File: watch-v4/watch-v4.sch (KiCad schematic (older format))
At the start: 33 parts, among them J1 CONN_10, P1 array connection, Q1 MOSFET_P, SW1 SPST, SW2 SPST, SW3 SPST, U1 IC_MCP73831, U2 MAX1722, U3 DS3231, U4 LSM9DS0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

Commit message: schematic cleanup, board work
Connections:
- net EXTVCC: now also D1.1 (A), R3.1
- net VCC: now also J1.4 (P4)
- net STAT: now reaches D2.2 (A), U1.1 (STAT)
- net Regulator_In: now reaches D1.2 (K), L1.1, Q1.3 (S), U2.1 (VIN)
- net Regulator_In: now also U2.3 (FB)
- net at C10.1, X1.3: now also U5.38 (XC1); no longer U5.37 (XC2)
- net at 12pf1.2, X1.1: now also U5.37 (XC2); no longer U5.38 (XC1)
- no-connect marks 1 -> 0
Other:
- moved on the sheet: C5, C6, C7, C8, D1, D2, L1, LIPOLY1, Q1, R1, R2, R3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

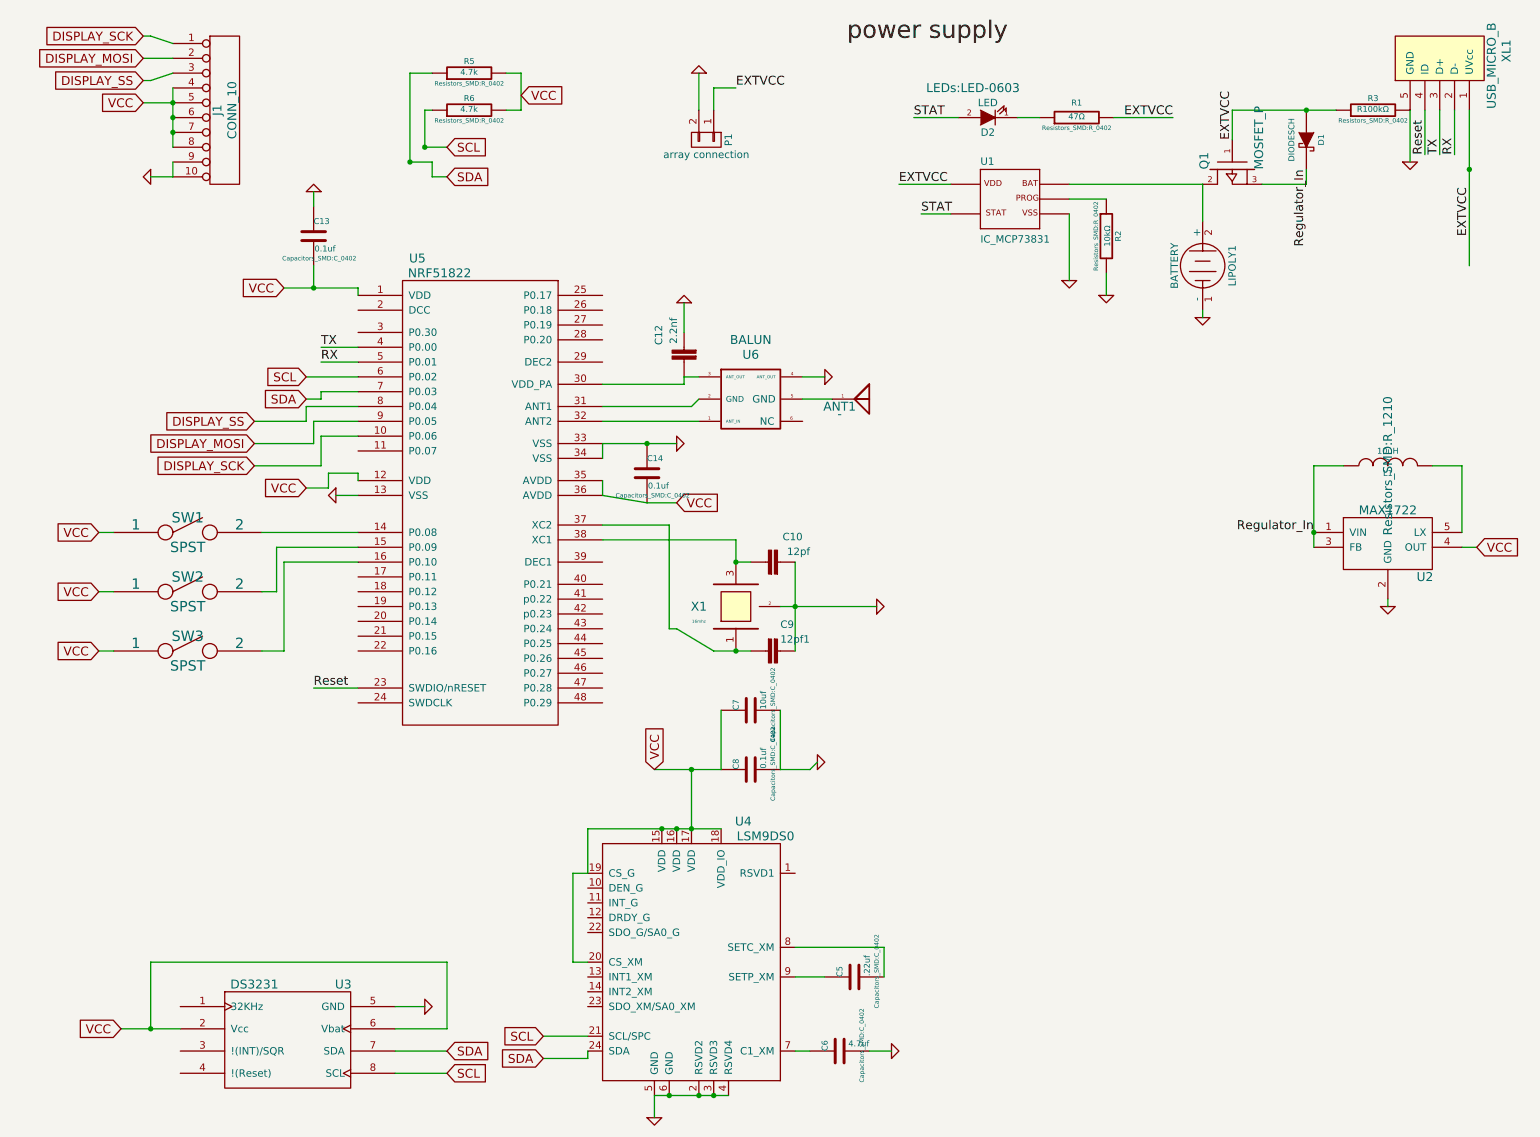
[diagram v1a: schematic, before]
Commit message: re-route board, redraw power supply in schematic
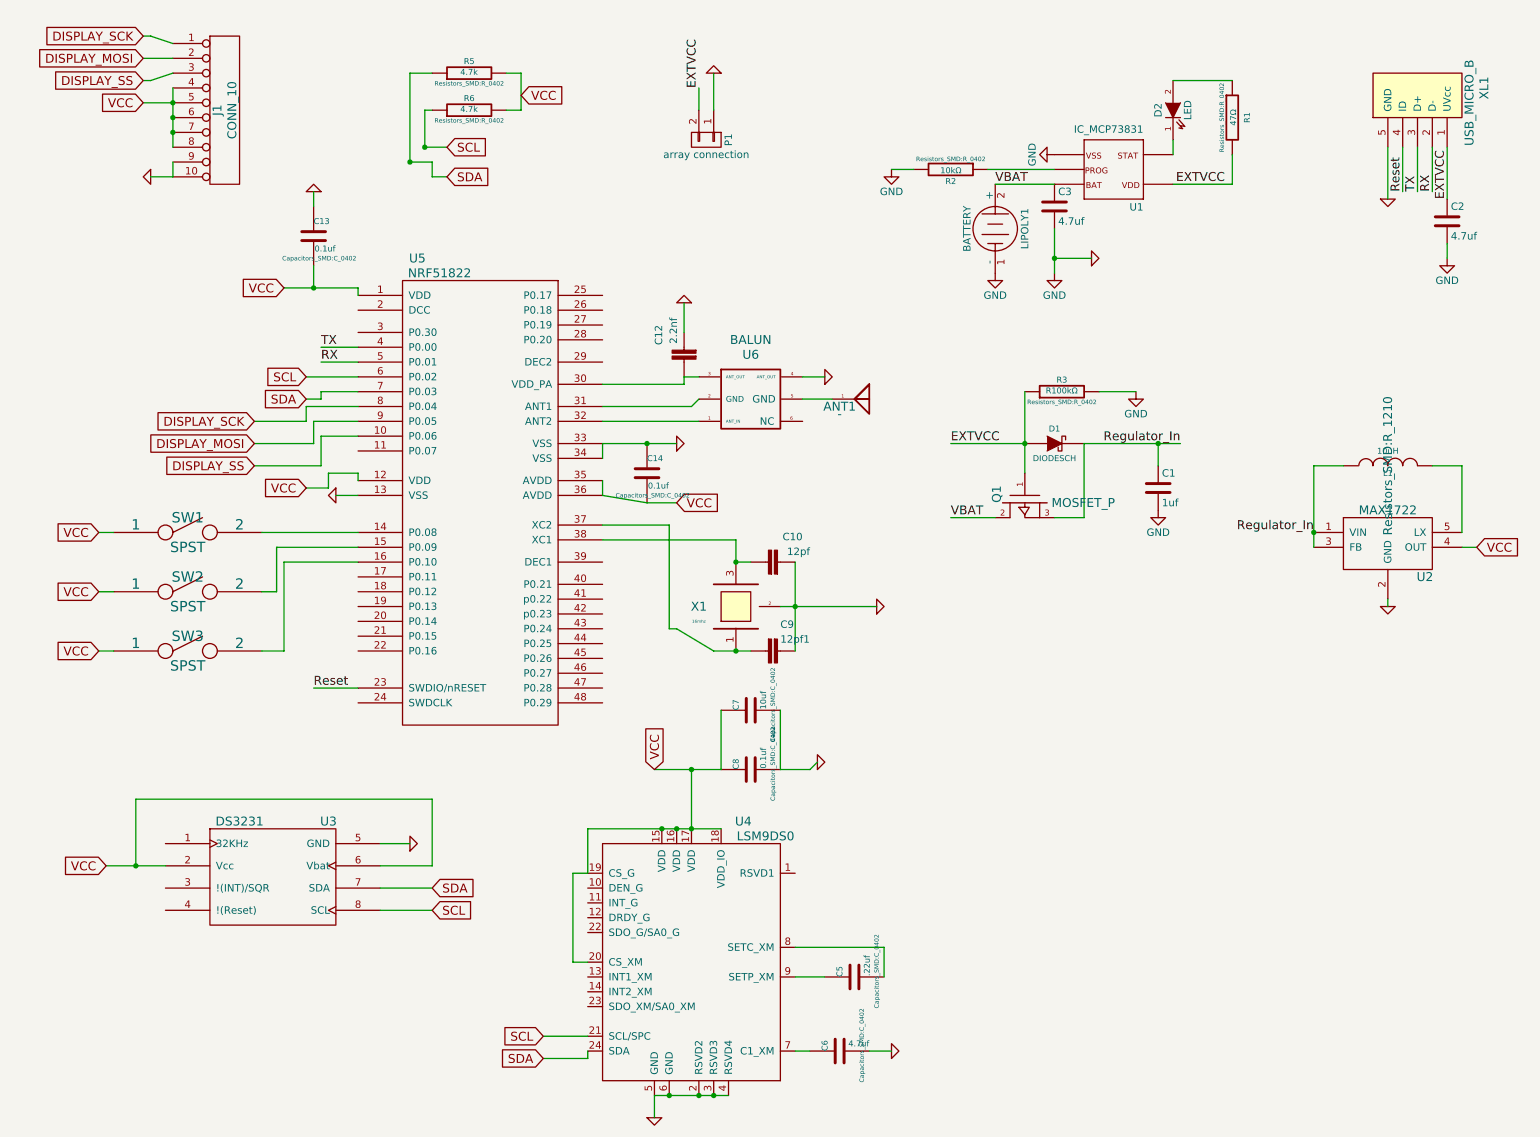
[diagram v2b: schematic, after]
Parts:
- added C1: 1uf, symbol C
- added C2, C3: 4.7uf, symbol C
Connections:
- net DISPLAY_SCK: now also U5.8 (P0.04); no longer U5.10 (P0.06)
- net DISPLAY_SS: now also U5.10 (P0.06); no longer U5.8 (P0.04)
- net EXTVCC: now also P1.2 (P2), C2.1; no longer P1.1 (P1)
- net GND: now also P1.1 (P1), C1.2, C2.2, C3.2; no longer P1.2 (P2)
- net Regulator_In: now also C1.1
- net VBAT: now reaches LIPOLY1.2 (+), Q1.2 (D), U1.3 (BAT)
- net VBAT: now also C3.1
- net at D2.1 (K): now also U1.1 (STAT); no longer R1.1
- net STAT: no longer names the net of D2.2 (A)
- net STAT: now also R1.1; no longer U1.1 (STAT)
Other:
- moved on the sheet: D1, D2, LIPOLY1, Q1, R1, R2, R3, U1, U3, XL1

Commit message: forgot to netlist the new parts; now with more caps, connections
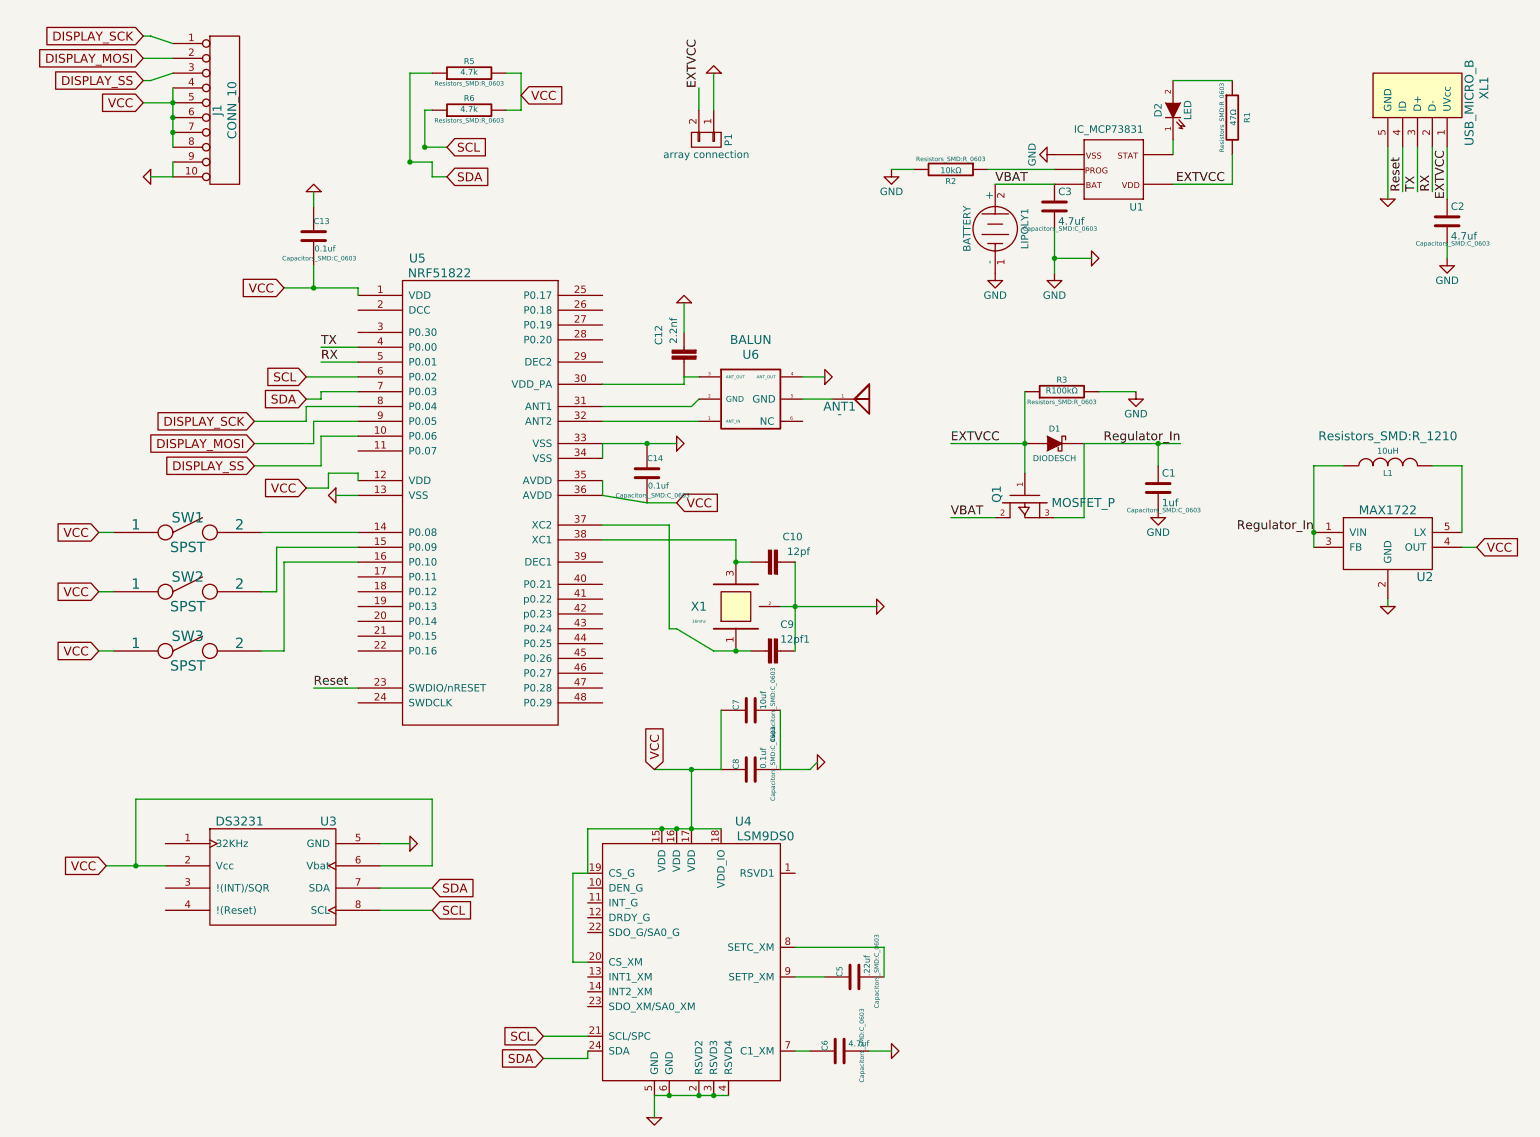
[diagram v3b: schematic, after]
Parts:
- 12pf1, C10, C12, C13, C14, C5, C6, C7, C8: footprint Capacitors_SMD:C_0402 -> Capacitors_SMD:C_0603
- C1, C2, C3: footprint (none) -> Capacitors_SMD:C_0603
- D1: footprint Diodes_SMD:Diode-SMA_Standard -> Diodes_SMD:SOD-123
- J1: footprint watch-v4:omron_XF2M-1015-1A -> watch-v4:omron_XF2M-1015-1A-2
- R1, R2, R3, R5, R6: footprint Resistors_SMD:R_0402 -> Resistors_SMD:R_0603
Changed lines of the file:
@@
 F 0 "R2" V 6730 1500 40  0000 C CNN
 F 1 "10kΩ" V 6657 1501 40  0000 C CNN
-F 2 "Resistors_SMD:R_0402" V 6580 1500 30  0000 C CNN
+F 2 "Resistors_SMD:R_0603" V 6580 1500 30  0000 C CNN
 F 3 "~" H 6650 1500 30  0000 C CNN
 	1    6650 1500
@@
 F 0 "R1" V 8650 1150 40  0000 C CNN
 F 1 "47Ω" V 8557 1151 40  0000 C CNN
-F 2 "Resistors_SMD:R_0402" V 8480 1150 30  0000 C CNN
+F 2 "Resistors_SMD:R_0603" V 8480 1150 30  0000 C CNN
 F 3 "~" H 8550 1150 30  0000 C CNN
 	1    8550 1150
@@
 F 0 "D1" H 7350 3450 40  0000 C CNN
 F 1 "DIODESCH" H 7350 3250 40  0000 C CNN
-F 2 "Diodes_SMD:Diode-SMA_Standard" H 7350 3350 60  0001 C CNN
+F 2 "Diodes_SMD:SOD-123" H 7350 3350 60  0001 C CNN
 F 3 "~" H 7350 3350 60  0000 C CNN
 	1    7350 3350
@@
 F 0 "R3" V 7480 3000 40  0000 C CNN
 F 1 "R100kΩ" V 7407 3001 40  0000 C CNN
-F 2 "Resistors_SMD:R_0402" V 7330 3000 30  0000 C CNN
+F 2 "Resistors_SMD:R_0603" V 7330 3000 30  0000 C CNN
 F 3 "~" H 7400 3000 30  0000 C CNN
 	1    7400 3000
@@
 F 0 "L1" V 9550 3500 40  0000 C CNN
 F 1 "10uH" V 9700 3500 40  0000 C CNN
-F 2 "Resistors_SMD:R_1210" H 9600 3500 60  0000 C CNN
+F 2 "Resistors_SMD:R_1210" V 9800 3500 60  0000 C CNN
 F 3 "~" H 9600 3500 60  0000 C CNN
 	1    9600 3500
@@
 F 0 "R5" V 3480 850 40  0000 C CNN
 F 1 "4.7k" V 3407 851 40  0000 C CNN
-F 2 "Resistors_SMD:R_0402" V 3330 850 30  0000 C CNN
+F 2 "Resistors_SMD:R_0603" V 3330 850 30  0000 C CNN
 F 3 "~" H 3400 850 30  0000 C CNN
 	1    3400 850
@@
 F 0 "R6" V 3480 1100 40  0000 C CNN
 F 1 "4.7k" V 3407 1101 40  0000 C CNN
-F 2 "Resistors_SMD:R_0402" V 3330 1100 30  0000 C CNN
+F 2 "Resistors_SMD:R_0603" V 3330 1100 30  0000 C CNN
 F 3 "~" H 3400 1100 30  0000 C CNN
 	1    3400 1100
@@
 F 0 "C5" H 6000 7050 40  0000 L CNN
 F 1 ".22uf" H 6006 6865 40  0000 L CNN
-F 2 "Capacitors_SMD:C_0402" H 6038 6800 30  0000 C CNN
+F 2 "Capacitors_SMD:C_0603" H 6038 6800 30  0000 C CNN
 F 3 "~" H 6000 6950 60  0000 C CNN
 	1    6000 6950
@@
 F 0 "C6" H 5900 7550 40  0000 L CNN
 F 1 "4.7uf" V 5950 7250 40  0000 L CNN
-F 2 "Capacitors_SMD:C_0402" H 5938 7300 30  0000 C CNN
+F 2 "Capacitors_SMD:C_0603" H 5938 7300 30  0000 C CNN
 F 3 "~" H 5900 7450 60  0000 C CNN
 	1    5900 7450
@@
 F 0 "C7" H 5300 5250 40  0000 L CNN
 F 1 "10uf" H 5306 5065 40  0000 L CNN
-F 2 "Capacitors_SMD:C_0402" H 5338 5000 30  0000 C CNN
+F 2 "Capacitors_SMD:C_0603" H 5338 5000 30  0000 C CNN
 F 3 "~" H 5300 5150 60  0000 C CNN
 	1    5300 5150
@@
 F 0 "C8" H 5300 5650 40  0000 L CNN
 F 1 "0.1uf" H 5306 5465 40  0000 L CNN
-F 2 "Capacitors_SMD:C_0402" H 5338 5400 30  0000 C CNN
+F 2 "Capacitors_SMD:C_0603" H 5338 5400 30  0000 C CNN
 F 3 "~" H 5300 5550 60  0000 C CNN
 	1    5300 5550
@@
 F 0 "J1" V 1700 1100 60  0000 C CNN
 F 1 "CONN_10" V 1800 1100 60  0000 C CNN
-F 2 "watch-v4:omron_XF2M-1015-1A" H 1750 1100 60  0001 C CNN
+F 2 "watch-v4:omron_XF2M-1015-1A-2" H 1750 1100 60  0001 C CNN
 F 3 "" H 1750 1100 60  0000 C CNN
 	1    1750 1100
@@
 F 0 "C10" V 5700 4000 50  0000 L BNN
 F 1 "12pf" V 5600 3950 50  0000 L BNN
-F 2 "Capacitors_SMD:C_0402" H 5500 4300 50  0001 C CNN
+F 2 "Capacitors_SMD:C_0603" H 5500 4300 50  0001 C CNN
 F 3 "" H 5500 4150 60  0000 C CNN
 	1    5500 4150
@@
 F 0 "12pf1" V 5350 4850 50  0000 L BNN
 F 1 "C9" V 5250 4850 50  0000 L BNN
-F 2 "Capacitors_SMD:C_0402" H 5400 4900 50  0001 C CNN
+F 2 "Capacitors_SMD:C_0603" H 5400 4900 50  0001 C CNN
 F 3 "" H 5400 4750 60  0000 C CNN
 	1    5400 4750
@@
 F 0 "C12" V 5050 2550 50  0000 L BNN
 F 1 "2.2nf" V 4950 2500 50  0000 L BNN
-F 2 "Capacitors_SMD:C_0402" H 4850 2850 50  0001 C CNN
+F 2 "Capacitors_SMD:C_0603" H 4850 2850 50  0001 C CNN
 F 3 "" H 4850 2700 60  0000 C CNN
 	1    4850 2700
@@
 F 0 "C13" H 2350 2050 40  0000 L CNN
 F 1 "0.1uf" H 2356 1865 40  0000 L CNN
-F 2 "Capacitors_SMD:C_0402" H 2388 1800 30  0000 C CNN
+F 2 "Capacitors_SMD:C_0603" H 2388 1800 30  0000 C CNN
 F 3 "~" H 2350 1950 60  0000 C CNN
 	1    2350 1950
@@
 F 0 "C14" H 4600 3650 40  0000 L CNN
 F 1 "0.1uf" H 4606 3465 40  0000 L CNN
-F 2 "Capacitors_SMD:C_0402" H 4638 3400 30  0000 C CNN
+F 2 "Capacitors_SMD:C_0603" H 4638 3400 30  0000 C CNN
 F 3 "~" H 4600 3550 60  0000 C CNN
 	1    4600 3550
@@
 F 0 "C2" H 10025 1950 50  0000 L CNN
 F 1 "4.7uf" H 10025 1750 50  0000 L CNN
-F 2 "" H 10038 1700 30  0000 C CNN
+F 2 "Capacitors_SMD:C_0603" H 10038 1700 30  0000 C CNN
 F 3 "" H 10000 1850 60  0000 C CNN
 	1    10000 1850
@@
 F 0 "C1" H 8075 3750 50  0000 L CNN
 F 1 "1uf" H 8075 3550 50  0000 L CNN
-F 2 "" H 8088 3500 30  0000 C CNN
+F 2 "Capacitors_SMD:C_0603" H 8088 3500 30  0000 C CNN
 F 3 "" H 8050 3650 60  0000 C CNN
 	1    8050 3650
@@
 F 0 "C3" H 7375 1850 50  0000 L CNN
 F 1 "4.7uf" H 7375 1650 50  0000 L CNN
-F 2 "" H 7388 1600 30  0000 C CNN
+F 2 "Capacitors_SMD:C_0603" H 7388 1600 30  0000 C CNN
 F 3 "" H 7350 1750 60  0000 C CNN
 	1    7350 1750
